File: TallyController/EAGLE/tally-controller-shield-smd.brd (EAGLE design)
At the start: 101.6 x 53.3 mm, 40 parts, among them J2 Mega R3, U1 SN75174N, U2 SN75174N, U3 SN75174N

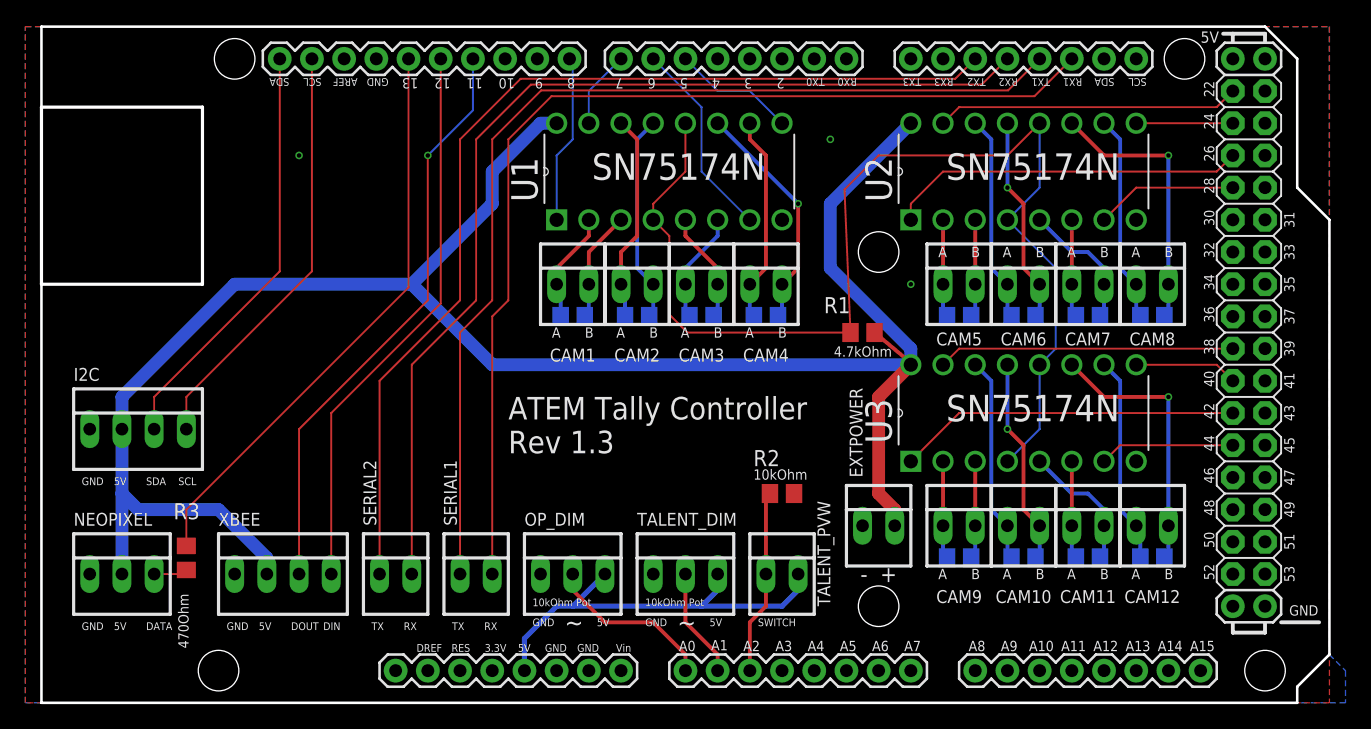
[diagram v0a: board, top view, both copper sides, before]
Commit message: Shift the RS485 drivers so they're aligned consistently
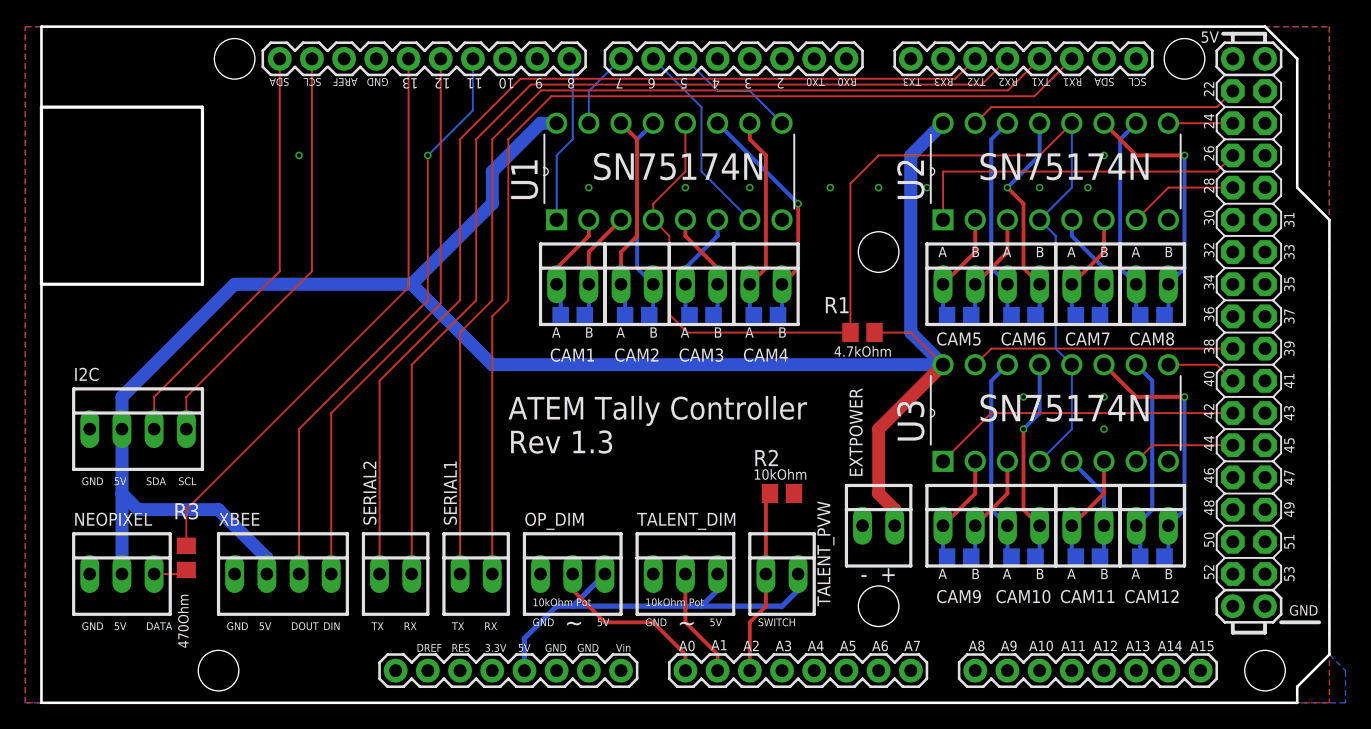
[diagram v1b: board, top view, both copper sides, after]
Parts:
- moved U2 2.54 mm to (88.9, 45.7)
- moved U3 2.54 mm to (88.9, 26.7)
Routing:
- net VCC: track 158.0 -> 161.0 mm
- net MEGA42: track 27.0 -> 24.4 mm
- net MEGA40: track 8.15 -> 5.61 mm
- net MEGA28: track 11.2 -> 8.67 mm
- net MEGA24: track 7.62 -> 5.08 mm
- net MEGA44: track 10.7 -> 8.15 mm
- net MEGA38: track 23.4 -> 20.8 mm
- net MEGA22: track 23.9 -> 21.4 mm
- net CAM11DB: track 10.6 -> 8.80 mm
- net CAM7DB: track 10.6 -> 8.80 mm
- net RS485EN: track 91.3 -> 92.6 mm
- net MEGA26: track 28.2 -> 27.2 mm
- net CAM9DB: track 7.75 -> 8.80 mm
- net CAM5DB: track 7.75 -> 8.80 mm
- net CAM7DA: track 7.75 -> 8.80 mm
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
